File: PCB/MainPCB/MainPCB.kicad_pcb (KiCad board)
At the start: 2 copper layers, 86.4 x 75.8 mm, 59 parts, among them J1 XT30PW-M, J10 JST-XH, J11 JST-XH, J12 XT30PW-M, J13 JST-XH, J14 JST-XH, J15 JST-XH, J16 XT30PW-M, J2 JST-XH, J3 JST-XH, J5 JST-XH, J6 JST-XH, J7 JST-XH, J8 JST-XH, J9 JST-XH, Q1 MTB7D0N6RJ3, Q2 MTB7D0N6RJ3, Q3 TJ60S04M3L, SW1 SW_Push, SW2 SW_DPST_x2, SW3 SW_Push, U1 Pico, U2 MCP1401T-E_OT, U3 MCP1401T-E_OT, U4 AZ1117CH-3.3TR

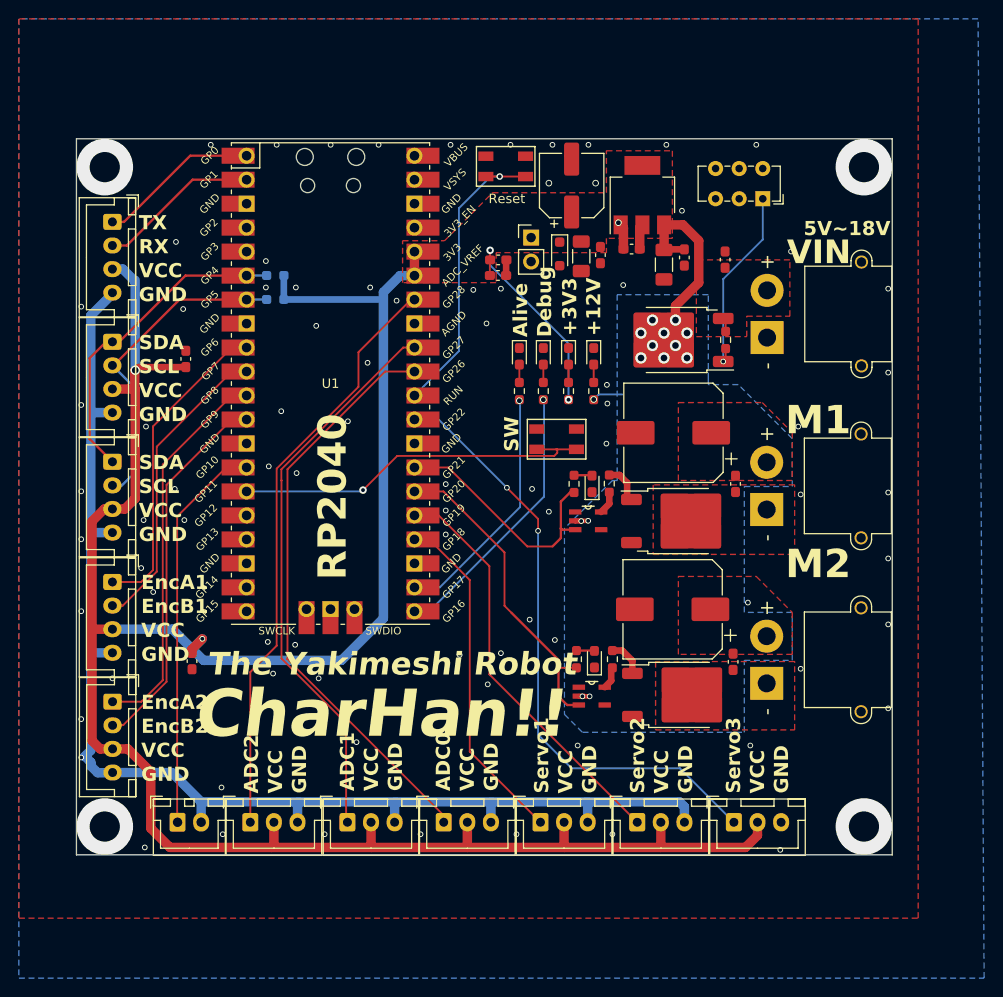
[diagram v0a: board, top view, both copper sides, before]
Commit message: :sparkles: フリーホイールダイオードを追加
# ==== Emojis ====
# ✨ :sparkles: Add new feature
# ✅  :white_check_mark: Update existing feature (not bug)
# ⚠️  :warning: Fix bug/error
# 🔥  :fire: Remove files or features
# ✏️ :pencil2: Fix typos
# 📝  :memo: Update documentation
# ♻️  :recycle: Dependencies update
# 🐧  :penguin: Improved the Linux
# 🍎  :apple: Improved the macOS
# 🔖 :bookmark: Add new library
# 🎉  :tada: Initial commit

# ==== Format ====
# :emoji: Subject
#
# Commit body...

# ==== Messages ====
# 新規(ファイル)機能追加: Add
# 機能修正、既存機能追加（バグではない): Update
# リファクタリング: Clean
# ファイル名変更:
# 削除など: Remove
# バグ修正: Fix
# バージョンアップ: Upgrade
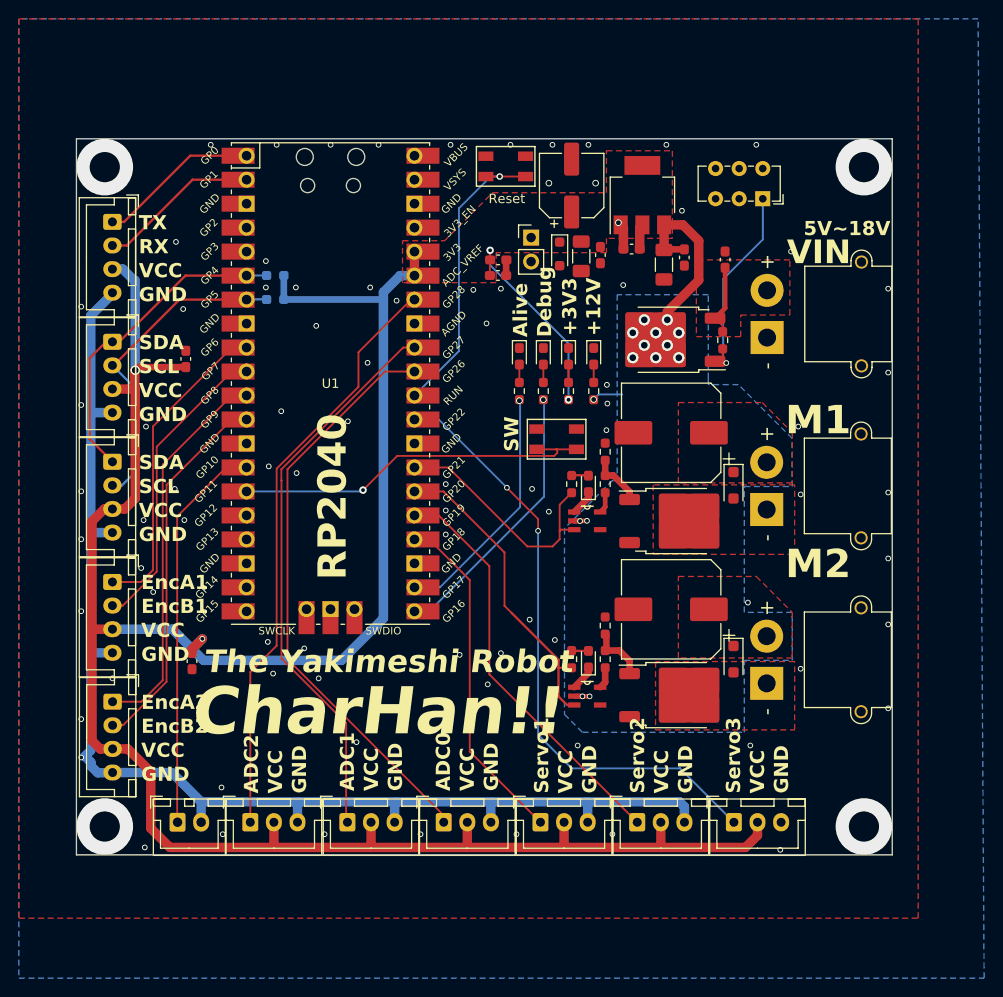
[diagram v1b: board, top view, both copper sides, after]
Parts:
- removed C1, C3: 0.1u, Capacitor_SMD:C_0603_1608Metric_Pad1.08x0.95mm_HandSolder
- added D8: ＧＳ１０１０ＦＬ, Diode_SMD:D_SOD-123F, F.Cu at (126.5, 87.5)
- added D9: D, Diode_SMD:D_SOD-123F, F.Cu at (126.5, 105.9)
- added R10: 10k, Resistor_SMD:R_0603_1608Metric_Pad0.98x0.95mm_HandSolder, F.Cu at (112.9, 102.4)
- added R13: 10k, Resistor_SMD:R_0603_1608Metric_Pad0.98x0.95mm_HandSolder, F.Cu at (112.9, 83.9)
- moved Q3 0.87 mm to (119.5, 72.1)
- moved R12 0.76 mm to (112.9, 105.9)
- moved D7 0.64 mm to (111.1, 105.9)
- moved R2 0.51 mm to (109.3, 105.9)
- moved U3 0.48 mm to (111.0, 109.8)
- moved R11 0.43 mm to (112.9, 87.4)
- moved D6 0.38 mm to (111.1, 87.4)
- moved R5 0.31 mm to (125.3, 72.1)
- moved Q2 0.30 mm to (120.5, 109.7)
- moved R1 0.26 mm to (109.3, 87.4)
- moved C4 0.24 mm to (119.9, 81.9)
- moved Q1 0.20 mm to (120.5, 91.3)
- moved C2 0.15 mm to (119.9, 100.6)
- moved U2 0.10 mm to (111.0, 91.3)
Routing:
- net +BATT: track 1.47 -> 7.54 mm
- net GND: track 140.6 -> 146.1 mm
- net Net-(Q2-G): track 4.03 -> 6.12 mm
- net Net-(Q1-G): track 3.82 -> 5.86 mm
- net +12V: track 32.0 -> 33.1 mm
- net MotorB: track 38.3 -> 37.6 mm

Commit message: :sparkles: Add PCB Production files
# ==== Emojis ====
# ✨ :sparkles: Add new feature
# ✅  :white_check_mark: Update existing feature (not bug)
# ⚠️  :warning: Fix bug/error
# 🔥  :fire: Remove files or features
# ✏️ :pencil2: Fix typos
# 📝  :memo: Update documentation
# ♻️  :recycle: Dependencies update
# 🐧  :penguin: Improved the Linux
# 🍎  :apple: Improved the macOS
# 🔖 :bookmark: Add new library
# 🎉  :tada: Initial commit

# ==== Format ====
# :emoji: Subject
#
# Commit body...

# ==== Messages ====
# 新規(ファイル)機能追加: Add
# 機能修正、既存機能追加（バグではない): Update
# リファクタリング: Clean
# ファイル名変更:
# 削除など: Remove
# バグ修正: Fix
# バージョンアップ: Upgrade
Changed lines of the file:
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@@
     (fp_line (start 1.6 0.8) (end -1.6 0.8)
       (stroke (width 0.1) (type solid)) (layer "F.Fab"))
-    (pad "1" smd roundrect (at -1.5625 0 270) (size 1.325 1.8) (layers "F.Cu" "F.Paste" "F.Mask") (roundrect_rratio 0.188679)
+    (pad "1" smd roundrect (at -1.5625 0 270) (size 1.325 1.8) (layers "F.Cu" "F.Paste" "F.Mask") (roundrect_rratio 0.1886792453)
       (net 5 "+3V3") (pintype "passive"))
-    (pad "2" smd roundrect (at 1.5625 0 270) (size 1.325 1.8) (layers "F.Cu" "F.Paste" "F.Mask") (roundrect_rratio 0.188679)
+    (pad "2" smd roundrect (at 1.5625 0 270) (size 1.325 1.8) (layers "F.Cu" "F.Paste" "F.Mask") (roundrect_rratio 0.1886792453)
       (net 3 "GND") (pintype "passive"))
     (model "${KICAD6_3DMODEL_DIR}/Capacitor_SMD.3dshapes/C_1206_3216Metric.wrl"

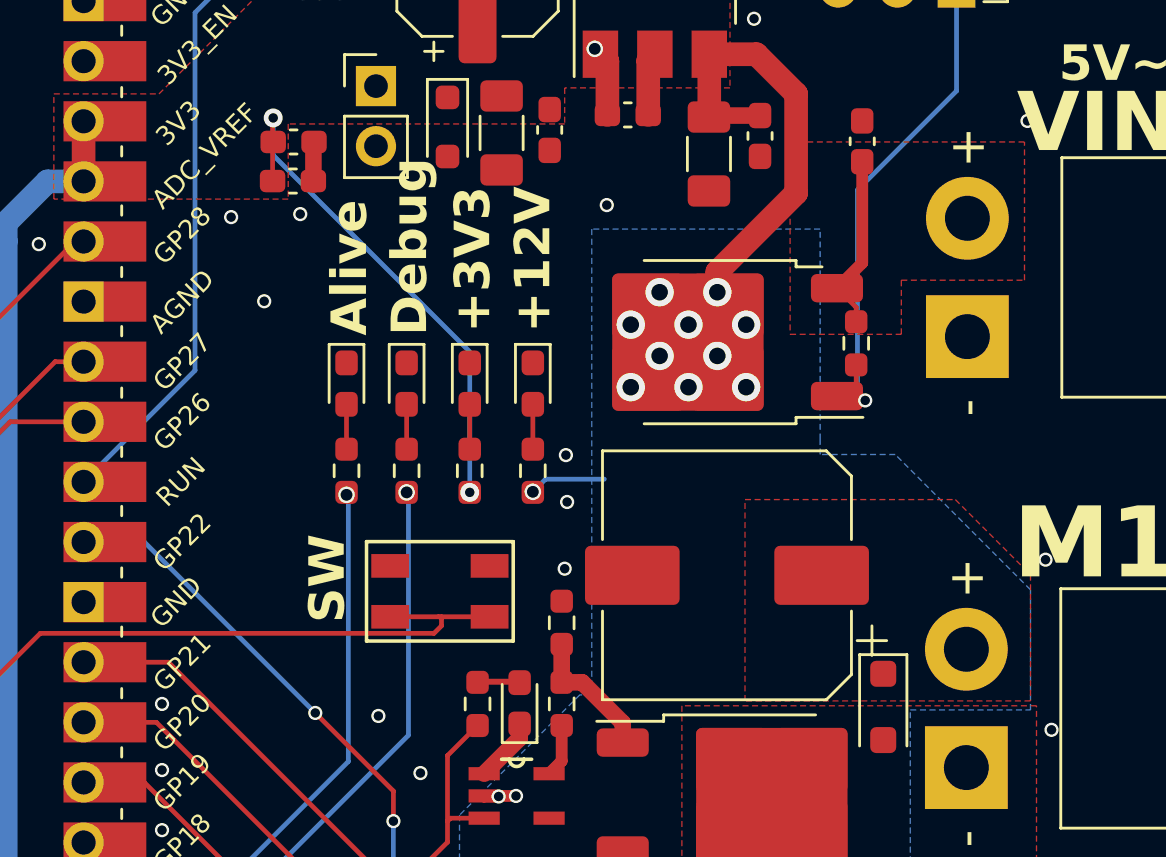
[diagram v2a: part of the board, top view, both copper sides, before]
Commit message: :sparkles: MDを作り始めた
# ==== Emojis ====
# ✨ :sparkles: Add new feature
# ✅  :white_check_mark: Update existing feature (not bug)
# ⚠️  :warning: Fix bug/error
# 🔥  :fire: Remove files or features
# ✏️ :pencil2: Fix typos
# 📝  :memo: Update documentation
# ♻️  :recycle: Dependencies update
# 🐧  :penguin: Improved the Linux
# 🍎  :apple: Improved the macOS
# 🔖 :bookmark: Add new library
# 🎉  :tada: Initial commit

# ==== Format ====
# :emoji: Subject
#
# Commit body...

# ==== Messages ====
# 新規(ファイル)機能追加: Add
# 機能修正、既存機能追加（バグではない): Update
# リファクタリング: Clean
# ファイル名変更:
# 削除など: Remove
# バグ修正: Fix
# バージョンアップ: Upgrade
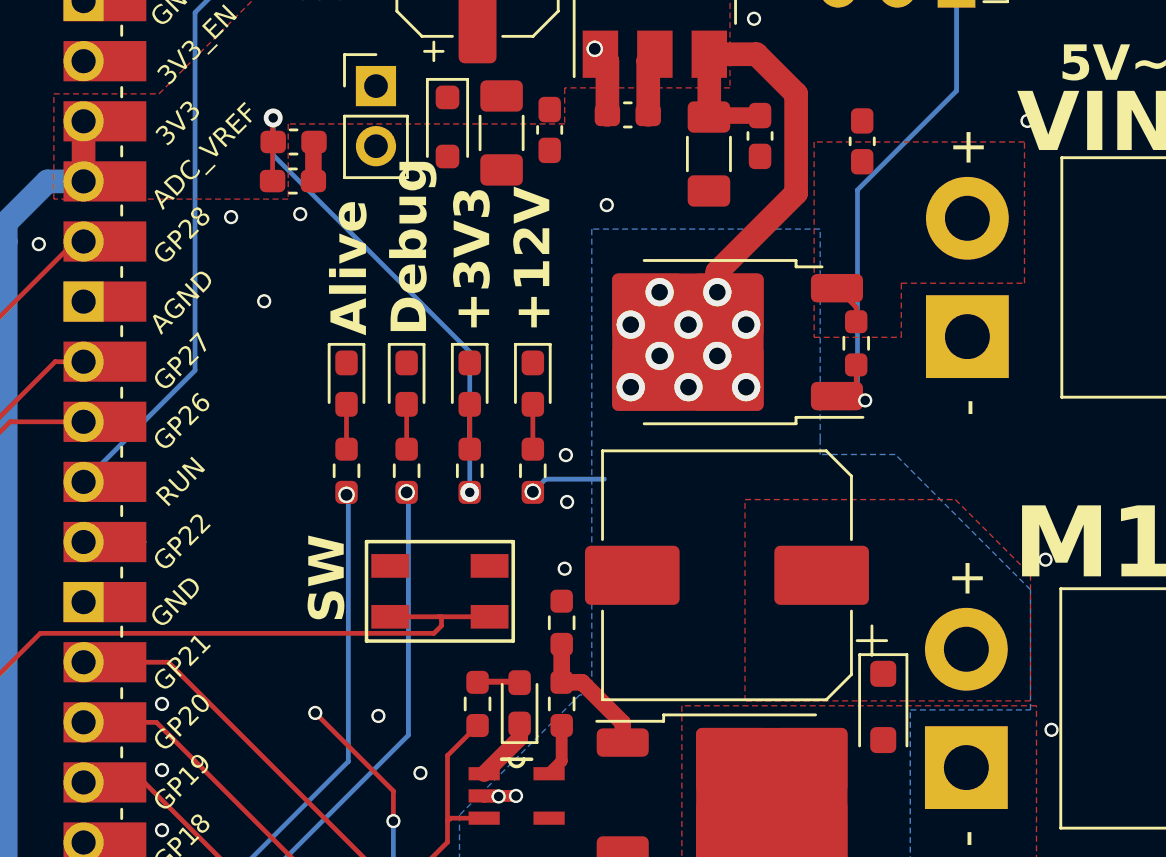
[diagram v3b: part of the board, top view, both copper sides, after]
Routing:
- net Servo3: track 64.9 -> 54.7 mm
- net +BATT: track 7.54 -> 1.75 mm
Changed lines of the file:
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@@
   (segment (start 74.918 72.913) (end 73.308 72.913) (width 0.25) (layer "F.Cu") (net 16))
   (segment (start 125.349 71.2235) (end 125.349 70.6182) (width 0.2) (layer "F.Cu") (net 17))
-  (segment (start 125.603 64.463) (end 125.603 68.7392) (width 0.5) (layer "F.Cu") (net 17))
-  (segment (start 125.603 68.7392) (end 124.5365 69.8057) (width 0.5) (layer "F.Cu") (net 17))
   (segment (start 125.349 70.6182) (end 124.5365 69.8057) (width 0.2) (layer "F.Cu") (net 17))
   (segment (start 72.756 85.613) (end 74.918 85.613) (width 0.2) (layer "F.Cu") (net 18))
@@
   (segment (start 105.791 113.919) (end 109.347 117.475) (width 0.2) (layer "B.Cu") (net 47))
   (segment (start 120.817 117.475) (end 126.532 123.19) (width 0.2) (layer "B.Cu") (net 47))
-  (segment (start 95.265 80.533) (end 102.489 87.757) (width 0.2) (layer "B.Cu") (net 47))
   (segment (start 111.0875 86.4382) (end 111.125 86.4757) (width 0.25) (layer "F.Cu") (net 48))
   (segment (start 109.600275 86.4382) (end 111.0875 86.4382) (width 0.25) (layer "F.Cu") (net 48))
@@
     )
   )
+  (zone (net 17) (net_name "+BATT") (layer "F.Cu") (name "+BATT") (hatch edge 0.5)
+    (priority 2)
+    (connect_pads thru_hole_only (clearance 0.2))
+    (min_thickness 0.25) (filled_areas_thickness no)
+    (fill yes (thermal_gap 0.5) (thermal_bridge_width 0.5))
+    (polygon
+      (pts
+        (xy 123.571 63.627)
+        (xy 123.571 71.882)
+        (xy 127.254 71.882)
+        (xy 127.254 69.596)
+        (xy 132.461 69.596)
+        (xy 132.461 63.627)
+      )
+    )
+  )
   (zone (net 7) (net_name "Net-(D3-A)") (layer "F.Cu") (name "$teardrop_padvia$") (hatch edge 0.5)
     (priority 30095)
@@
       )
     )
-  )
-  (zone (net 17) (net_name "+BATT") (layer "F.Cu") (name "12V") (hatch edge 0.5)
-    (priority 3)
-    (connect_pads no (clearance 0.2))
-    (min_thickness 0.25) (filled_areas_thickness no)
-    (fill yes (thermal_gap 0.5) (thermal_bridge_width 0.5))
-    (polygon
-      (pts
-        (xy 127.254 71.755)
-        (xy 127.254 69.469)
-        (xy 132.461 69.469)
-        (xy 132.461 63.627)
-        (xy 122.555 63.627)
-        (xy 122.555 71.755)
-      )
-    )
